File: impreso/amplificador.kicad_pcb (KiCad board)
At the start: 2 copper layers, 92 parts, among them Q1 2SC3281, Q10 MPSA42, Q11 2SC3281, Q12 2SA1302, Q13 MPSA92, Q14 MPSA92, Q15 MJE340, Q16 MJE350, Q17 MJE350, Q2 MJE340, Q20 2SA1302, Q3 MJE340, Q4 2SC3281, Q5 MJE340, Q6 MJE350, Q7 2SA1302, Q8 MJE350, Q9 MPSA42, T3 TORNILLO, T4 TORNILLO, T5 TORNILLO, T6 TORNILLO, T7 TORNILLO, T8 TORNILLO, U1 MMPQ2222A, U2 MMPQ2907A, U3 LM7809CT, U4 LM7909CT

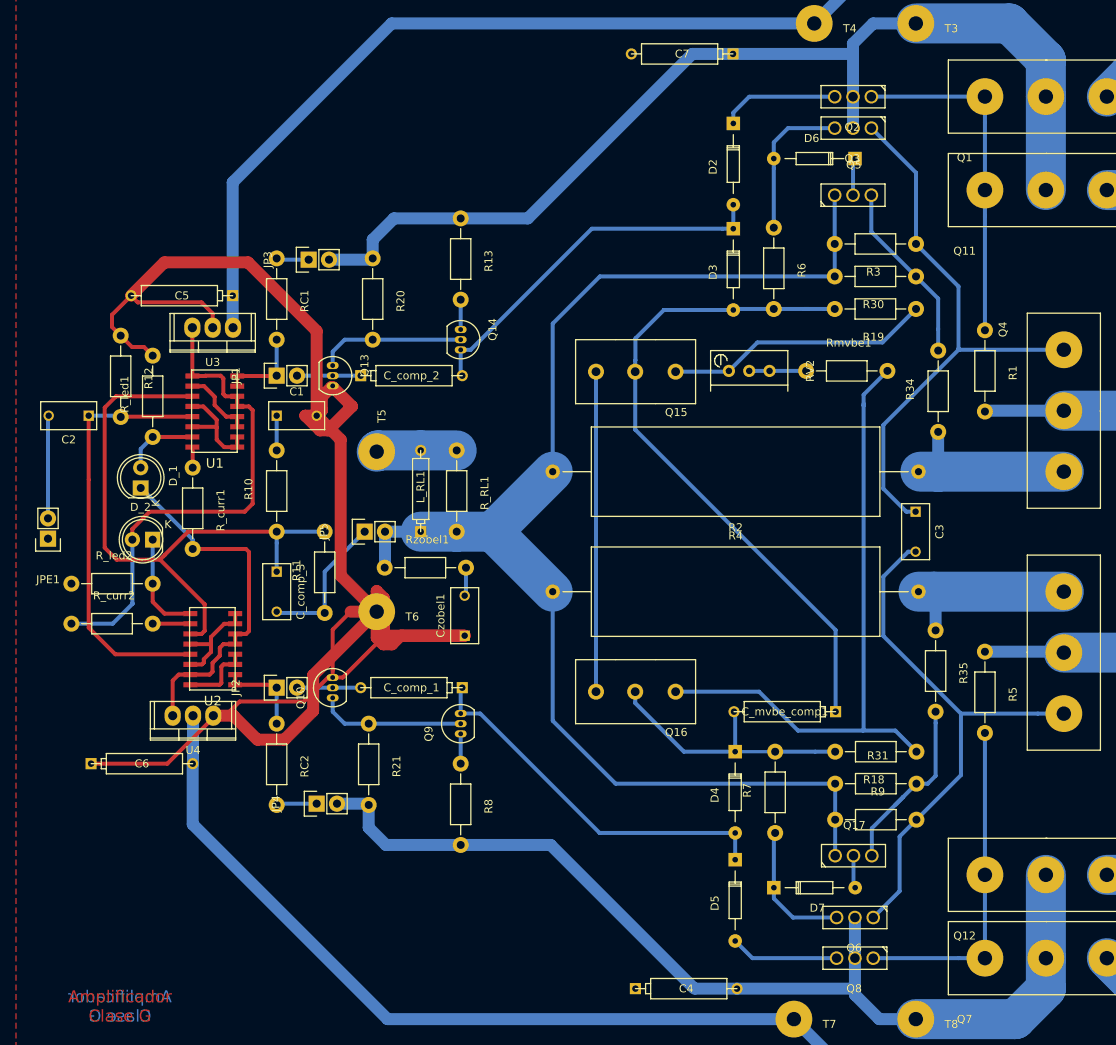
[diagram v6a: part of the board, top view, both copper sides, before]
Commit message: Ensanché las vías del PCB y agregué un par de vías.
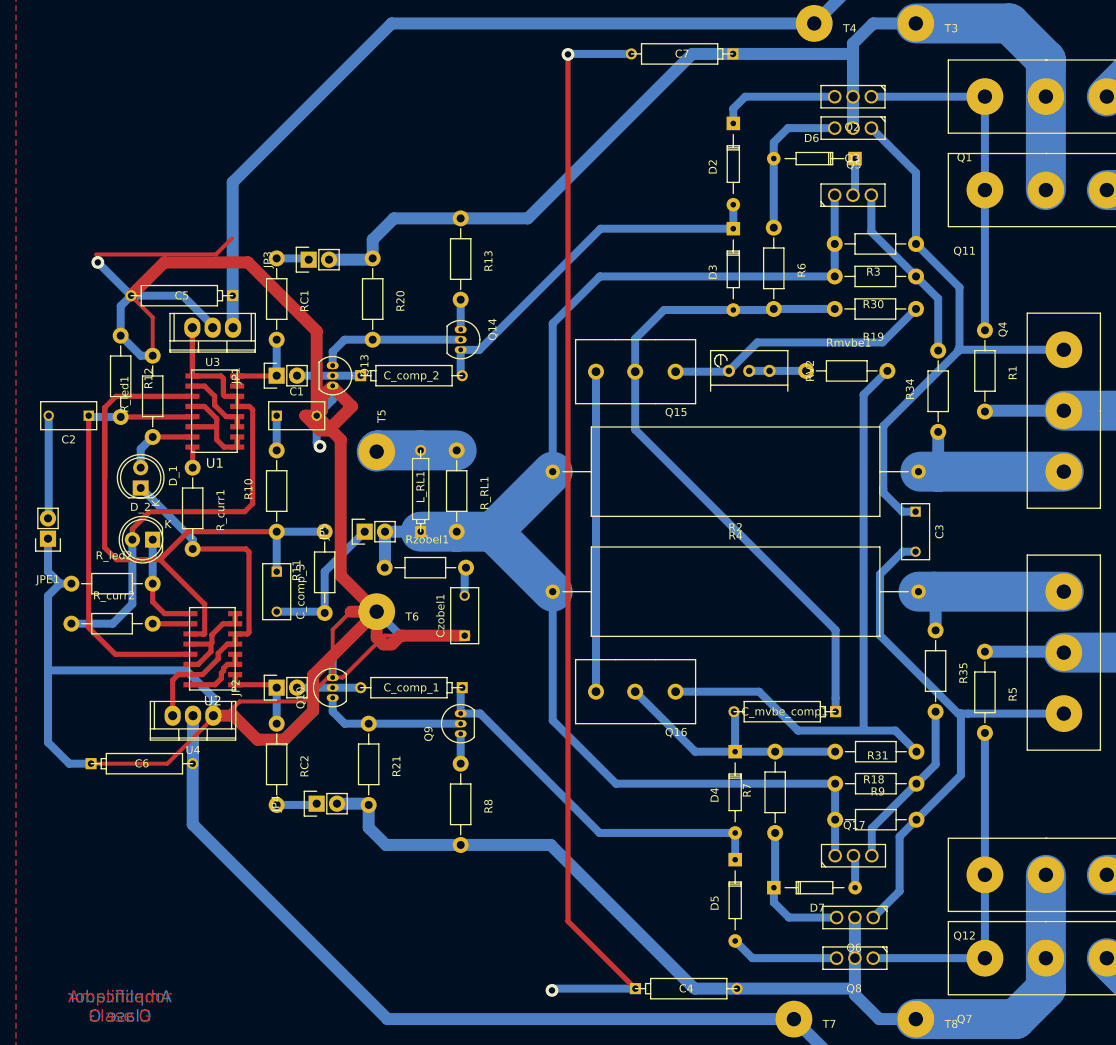
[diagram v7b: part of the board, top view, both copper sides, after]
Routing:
- net SalidaGND: track 239.6 -> 480.5 mm, vias 0 -> 5
- net Net-(Q16-Pad3): track 79.7 -> 133.3 mm
- net Net-(C3-Pad1): track 71.9 -> 122.2 mm
- net Net-(C_comp_3-Pad1): track 77.3 -> 95.0 mm
- net Net-(Q1-Pad1): track 43.4 -> 57.6 mm
- net Net-(C_mvbe_comp1-Pad1): track 84.3 -> 91.9 mm
- net Net-(Q17-Pad3): track 23.7 -> 30.8 mm
- net Net-(C_mvbe_comp1-Pad2): track 34.5 -> 38.6 mm
- net Net-(U1-Pad1): track 13.5 -> 16.1 mm
- net Net-(Q10-Pad1): track 18.3 -> 20.1 mm
- net Net-(C3-Pad2): track 69.4 -> 70.3 mm
- net Net-(D_1-Pad1): track 45.9 -> 46.7 mm
- net Net-(U2-Pad16): track 9.13 -> 8.50 mm
